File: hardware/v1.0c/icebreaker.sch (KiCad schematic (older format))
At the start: 124 parts, among them J1 Jumper, J10 Jumper, J11 Jumper, J12 Jumper, J13 Jumper, J14 Jumper, J15 Jumper, J16 Jumper, J17 Jumper, J18 Jumper, J19 Jumper, J2 Jumper, J20 Flash, J21 PMOD, J22 PMOD, J23 PMOD, J24 PMOD, J25 RGB Led, J26 5V AUX, J27 5V AUX, J28 CRESET, J29 Jumper, J3 Jumper, J30 Jumper, J4 Jumper, J5 Jumper, J6 Jumper, J7 Jumper, J8 Jumper, J9 Jumper, P1 pkl_USB_OTG, P2 UP, P3 UP, P4 UP, P5 UP, P6 RAM_CS, SW1 TACT, SW2 TACT, SW3 TACT, SW4 TACT, U1 93C46B-SOT-23-6, U2 3.3V, U3 1V2, U4 FT2232H, U5 W25Q, U6 ICE5LP4K-SG48, U7 12MHz

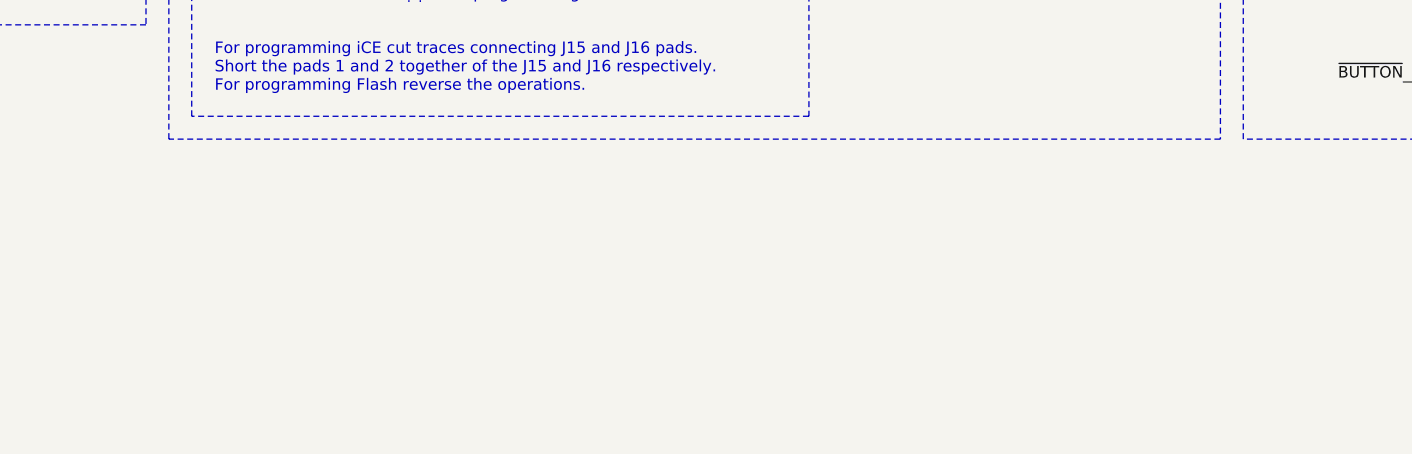
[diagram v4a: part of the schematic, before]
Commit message: Added "ear" circuits. WS2812 & Shitty Addon.
The "top" ear is a RGB LED connector to WS2812 adapter with level
shifting to 5V. It supports one WS2812 string interface. (there is not
enough space for more channels unfortunately.

The "bottom" ear is a RGB LED connector to Shitty Addon adapter with I2C
pullups. This allows for connecting badgelife shitty addon mini badges
to the iCEBreaker.
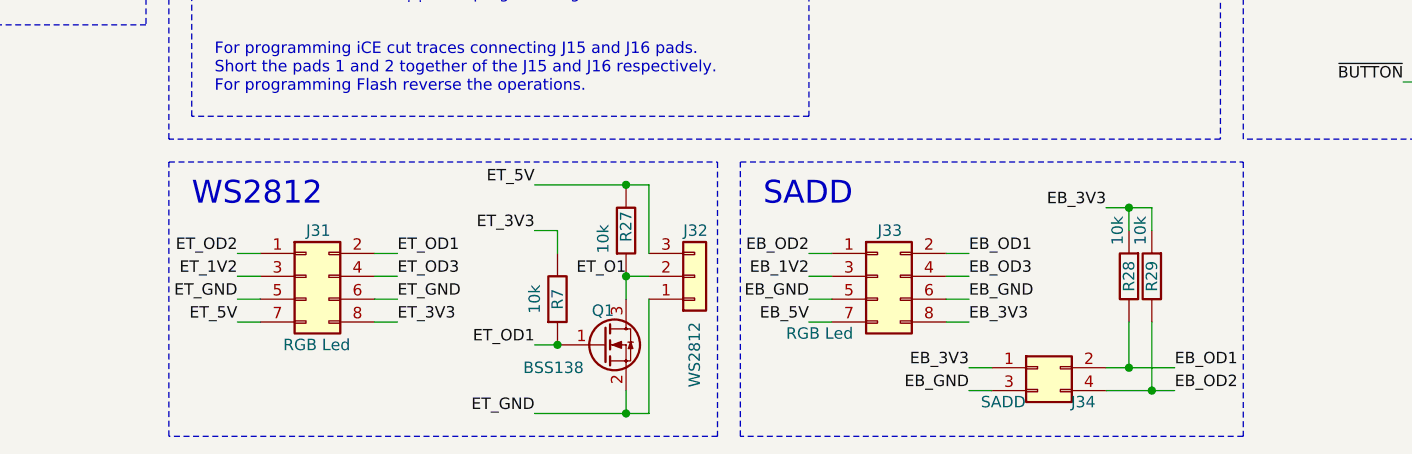
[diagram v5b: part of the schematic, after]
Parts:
- added J31, J33: RGB Led, Connector_PinSocket_2.54mm:PinSocket_2x04_P2.54mm_Vertical, symbol Connector_Generic:Conn_02x04_Odd_Even
- added J32: WS2812, Connector_PinHeader_2.54mm:PinHeader_1x03_P2.54mm_Vertical, symbol Connector_Generic:Conn_01x03
- added J34: SADD, Connector_PinSocket_2.54mm:PinSocket_2x02_P2.54mm_Vertical, symbol Connector_Generic:Conn_02x02_Odd_Even
- added Q1: BSS138, Package_TO_SOT_SMD:SOT-23, symbol pkl_device:pkl_Q_NMOS_BD_GSD
- added R27, R28, R29, R7: 10k, pkl_dipol:R_0603, symbol pkl_device:pkl_R
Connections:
- new net EB_1V2: J33.3 (Pin_3)
- new net EB_3V3: J33.8 (Pin_8), J34.1 (Pin_1), R28.2, R29.2
- new net EB_5V: J33.7 (Pin_7)
- new net EB_GND: J33.5 (Pin_5), J33.6 (Pin_6), J34.3 (Pin_3)
- new net EB_OD1: J33.2 (Pin_2), J34.2 (Pin_2), R28.1
- new net EB_OD2: J33.1 (Pin_1), J34.4 (Pin_4), R29.1
- new net EB_OD3: J33.4 (Pin_4)
- new net ET_1V2: J31.3 (Pin_3)
- new net ET_3V3: J31.8 (Pin_8), R7.1
- new net ET_5V: J31.7 (Pin_7), J32.3 (Pin_3), R27.1
- new net ET_GND: J31.5 (Pin_5), J31.6 (Pin_6), J32.1 (Pin_1), Q1.2 (S)
- new net ET_O1: J32.2 (Pin_2), Q1.3 (D), R27.2
- new net ET_OD1: J31.2 (Pin_2), Q1.1 (G), R7.2
- new net ET_OD2: J31.1 (Pin_1)
- new net ET_OD3: J31.4 (Pin_4)
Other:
- note added: "SADD"
- note added: "WS2812"

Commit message: Added DNP markers to the newly added footprints and ears.
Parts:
- Q1, R27, R28, R29, R7: DNP (none) -> YES
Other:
- note added: "Unpopulated"
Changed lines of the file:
@@
 F 2 "Package_TO_SOT_SMD:SOT-23" H 9100 10900 50  0001 C CNN
 F 3 "~" H 8900 10800 50  0001 C CNN
+F 4 "YES" H 8900 10800 50  0001 C CNN "DNP"
 	1    8900 10800
 	1    0    0    -1
@@
 F 4 "res-0402-10k" H -2500 5200 50  0001 C CNN "Key"
 F 5 "ANY" H 8700 10600 50  0001 C CNN "Source"
+F 6 "YES" H 8700 10600 50  0001 C CNN "DNP"
 	1    8700 10600
 	1    0    0    -1
@@
 F 4 "res-0402-10k" H -2200 4900 50  0001 C CNN "Key"
 F 5 "ANY" H 9000 10300 50  0001 C CNN "Source"
+F 6 "YES" H 9000 10300 50  0001 C CNN "DNP"
 	1    9000 10300
 	1    0    0    -1
@@
 F 4 "res-0402-10k" H 0   5100 50  0001 C CNN "Key"
 F 5 "ANY" H 11200 10500 50  0001 C CNN "Source"
+F 6 "YES" H 11200 10500 50  0001 C CNN "DNP"
 	1    11200 10500
 	-1   0    0    1
@@
 F 4 "res-0402-10k" H 100 5100 50  0001 C CNN "Key"
 F 5 "ANY" H 11300 10500 50  0001 C CNN "Source"
+F 6 "YES" H 11300 10500 50  0001 C CNN "DNP"
 	1    11300 10500
 	-1   0    0    1
@@
 	11200 10200 11100 10200
 Connection ~ 11200 10200
+Text Notes 9550 11150 0    75   ~ 0
+Unpopulated
+Text Notes 7050 11150 0    75   ~ 0
+Unpopulated
+Text Notes 15250 9850 0    75   ~ 0
+Unpopulated
 $EndSCHEMATC

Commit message: Added "Ear" legend in the schamatic.
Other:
- note added: "SADD "Ear""
- note added: "WS2812 "Ear""
- note removed: "SADD"
- note removed: "WS2812"
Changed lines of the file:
@@
 EB_OD2
 Text Notes 7100 10200 0    100  ~ 0
-WS2812
+WS2812 "Ear"
 Text Notes 9600 10200 0    100  ~ 0
-SADD
+SADD "Ear"
 Wire Notes Line
 	9500 10000 11700 10000
